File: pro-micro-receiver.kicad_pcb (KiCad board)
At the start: 4 copper layers, 40 parts, among them J1 USB_A_PLUG, J2 Conn_01x04, SW1 SW_Push, U1 TLV740P, U2 ATmega32U4-M, U3 YJ-14015, Y1 16MHz

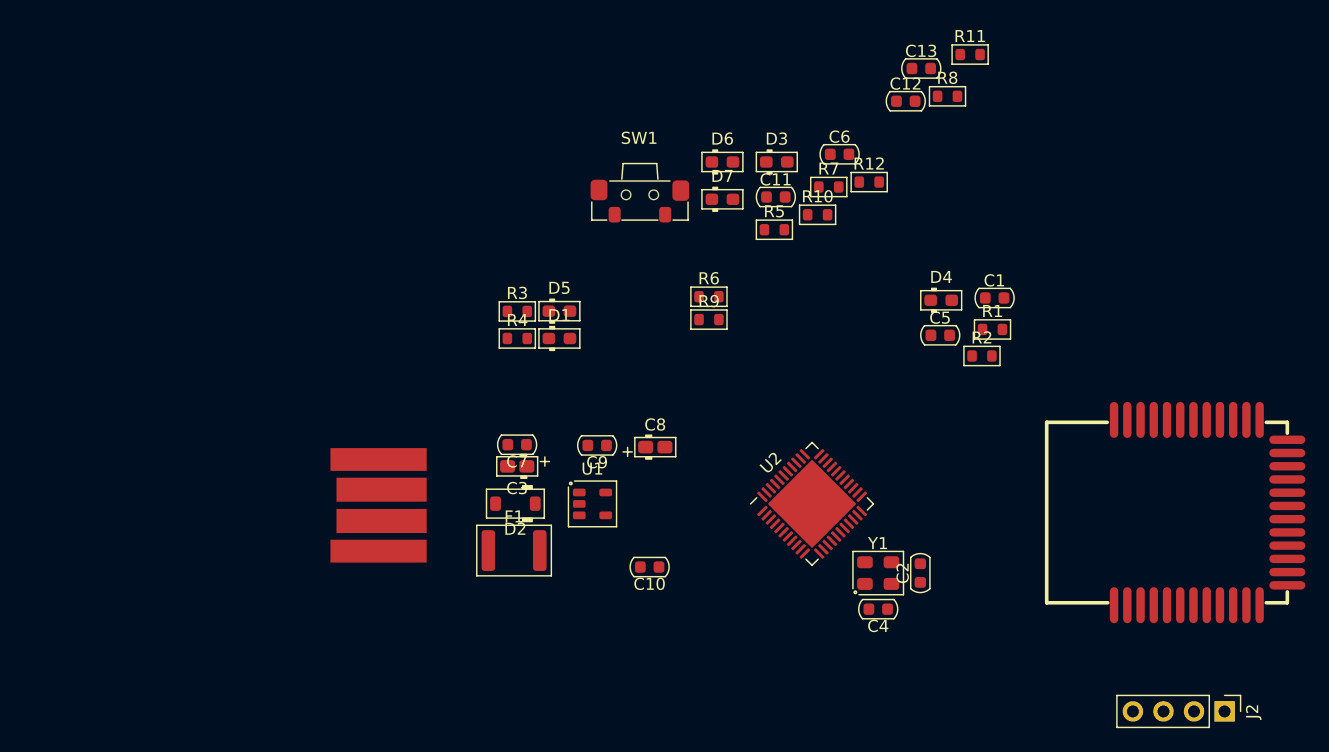
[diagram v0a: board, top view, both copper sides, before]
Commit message: Fixing the stackup Adding initial board outline Moving all elements onto the board
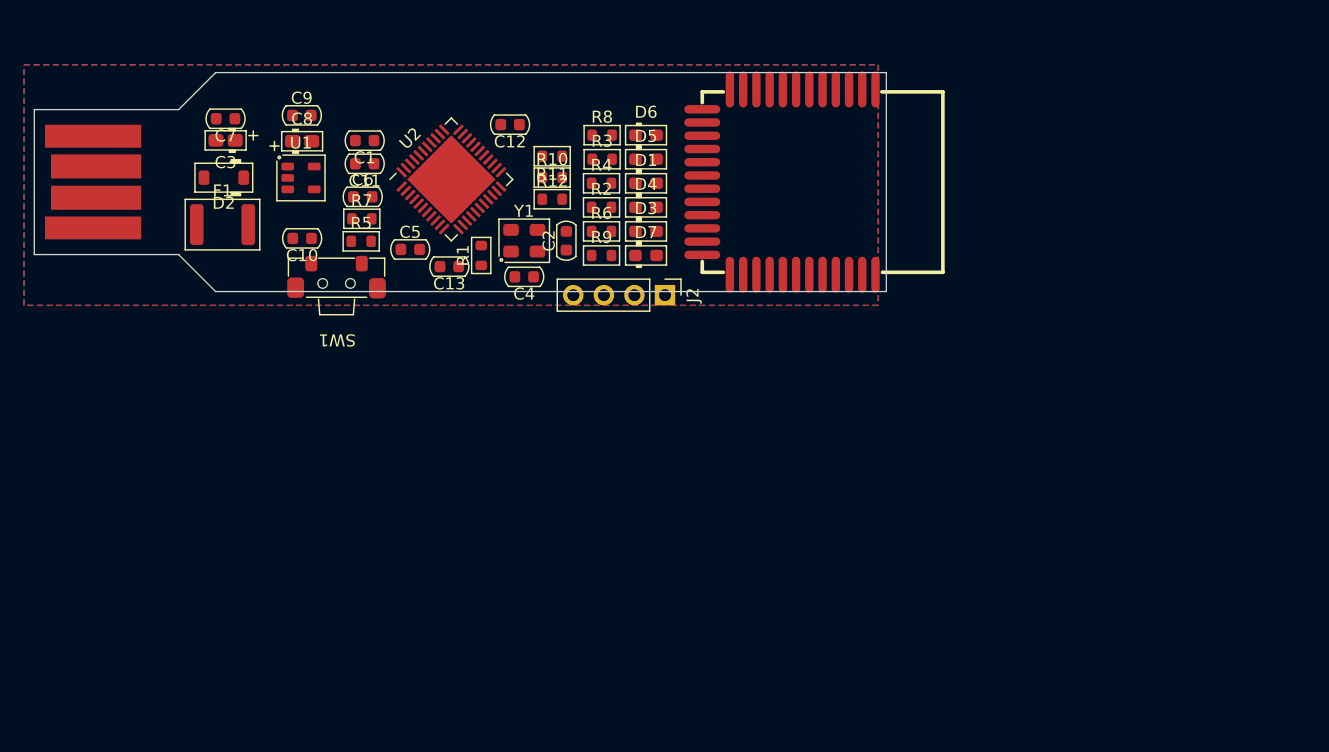
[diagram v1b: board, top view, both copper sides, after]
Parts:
- moved J2 58.0 mm to (113.3, 83.2)
- moved C1 54.0 mm to (88.3, 70.3), turned to 180 degrees
- moved C5 44.6 mm to (92.1, 79.3)
- moved R1 42.9 mm to (98.0, 79.8), turned to 90 degrees
- moved C13 42.5 mm to (95.3, 80.8), turned to 180 degrees
- moved C2 40.4 mm to (105.1, 78.6)
- moved C4 40.4 mm to (101.6, 81.6)
- moved Y1 40.4 mm to (101.6, 78.6)
- moved U2 40.3 mm to (95.5, 73.5)
- moved C6 39.8 mm to (88.2, 75.0)
- moved C10 39.8 mm to (83.1, 78.4)
- moved R7 38.9 mm to (88.1, 76.8)
- moved C8 38.8 mm to (83.1, 70.4)
- moved C9 36.8 mm to (83.1, 68.2), turned to 0 degrees
- moved C3 36.4 mm to (76.8, 70.3)
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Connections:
- net Net-(R5-Pad1) renamed /D+OUT
- net Net-(R7-Pad1) renamed /D-OUT
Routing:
- added copper zone on B.Cu, net GND
- added copper zone on F.Cu, net GND
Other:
- board outline added: 70.8 x 18.2 mm

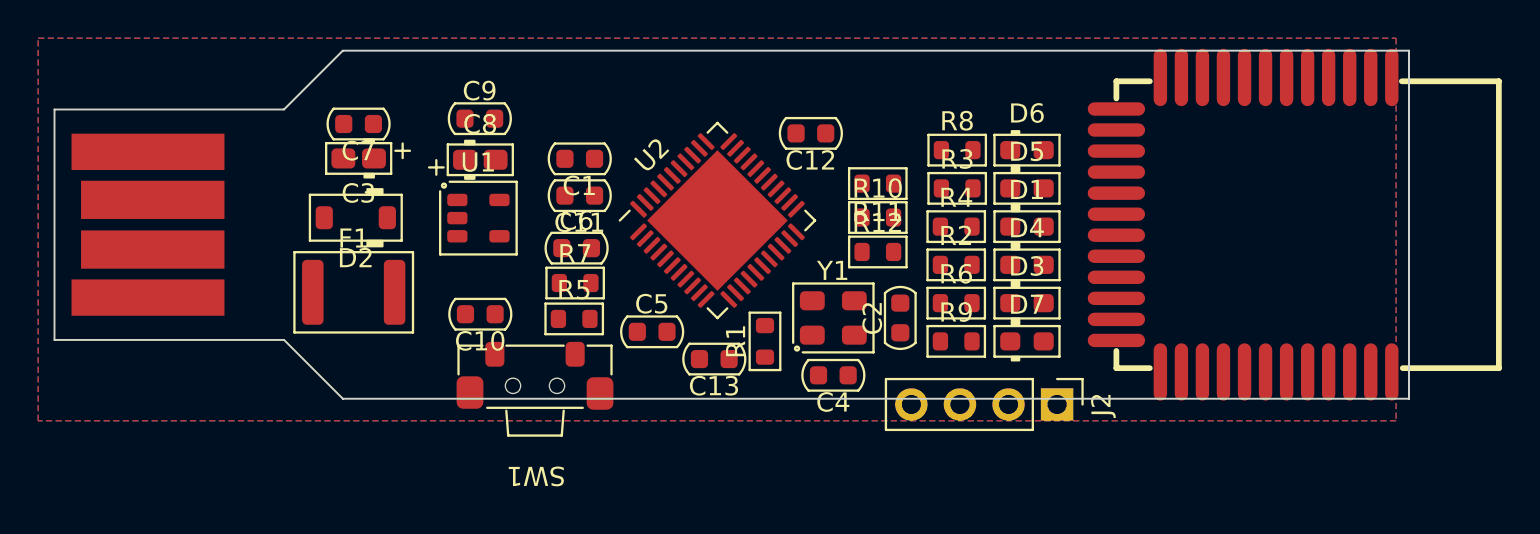
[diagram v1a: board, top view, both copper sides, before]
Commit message: Shortening the board and better placement of components
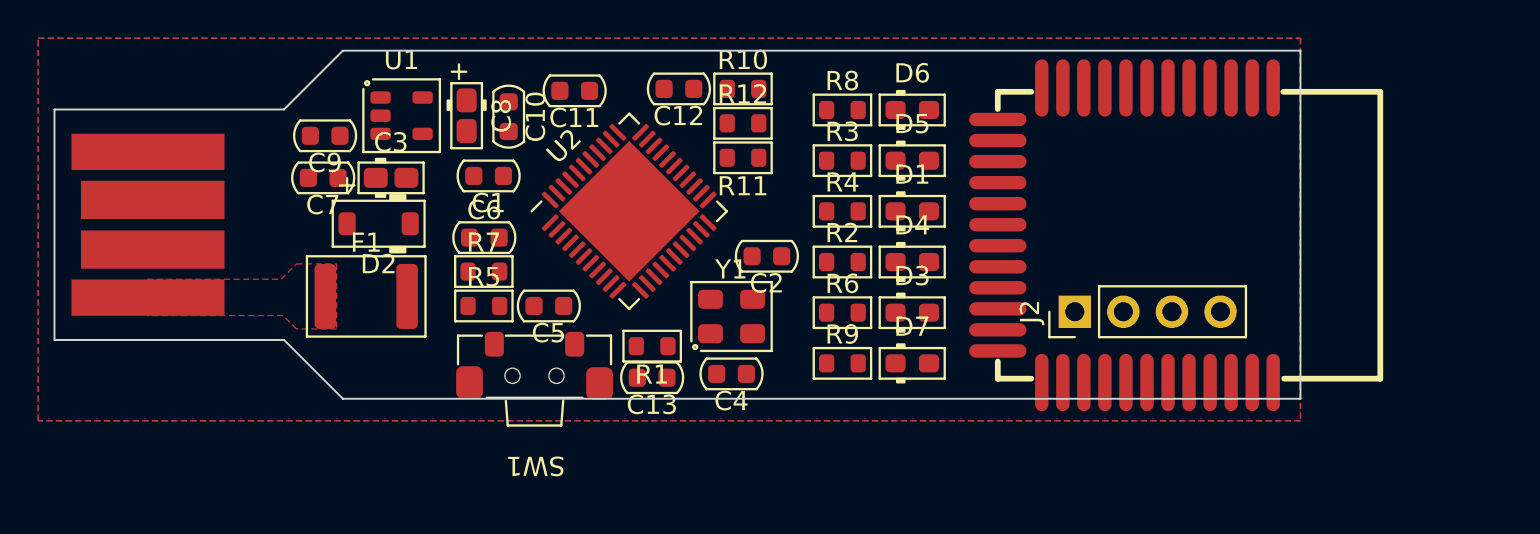
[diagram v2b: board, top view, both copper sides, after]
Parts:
- moved C10 10.4 mm to (84.6, 68.1), turned to -90 degrees
- moved R10 9.74 mm to (96.8, 66.7)
- moved R12 9.74 mm to (96.8, 68.5)
- moved C9 8.14 mm to (75.0, 69.1), turned to 180 degrees
- moved C2 7.68 mm to (98.1, 75.4), turned to 180 degrees
- moved C12 7.28 mm to (93.5, 66.7)
- moved R11 7.18 mm to (96.8, 70.2)
- moved U1 6.69 mm to (79.0, 68.0)
- moved D6 6.36 mm to (105.7, 67.8)
- moved R8 6.36 mm to (102.0, 67.8)
- moved U3 6.22 mm to (130.2, 74.3)
- moved D5 6.17 mm to (105.7, 70.4)
- moved R3 6.17 mm to (102.0, 70.4)
- moved D7 6.11 mm to (105.7, 81.0)
- moved R9 6.06 mm to (102.0, 81.0)
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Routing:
- added copper zone on F.Cu, net UVCC
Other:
- board size 70.8 x 18.2 mm -> 65.2 x 18.2 mm

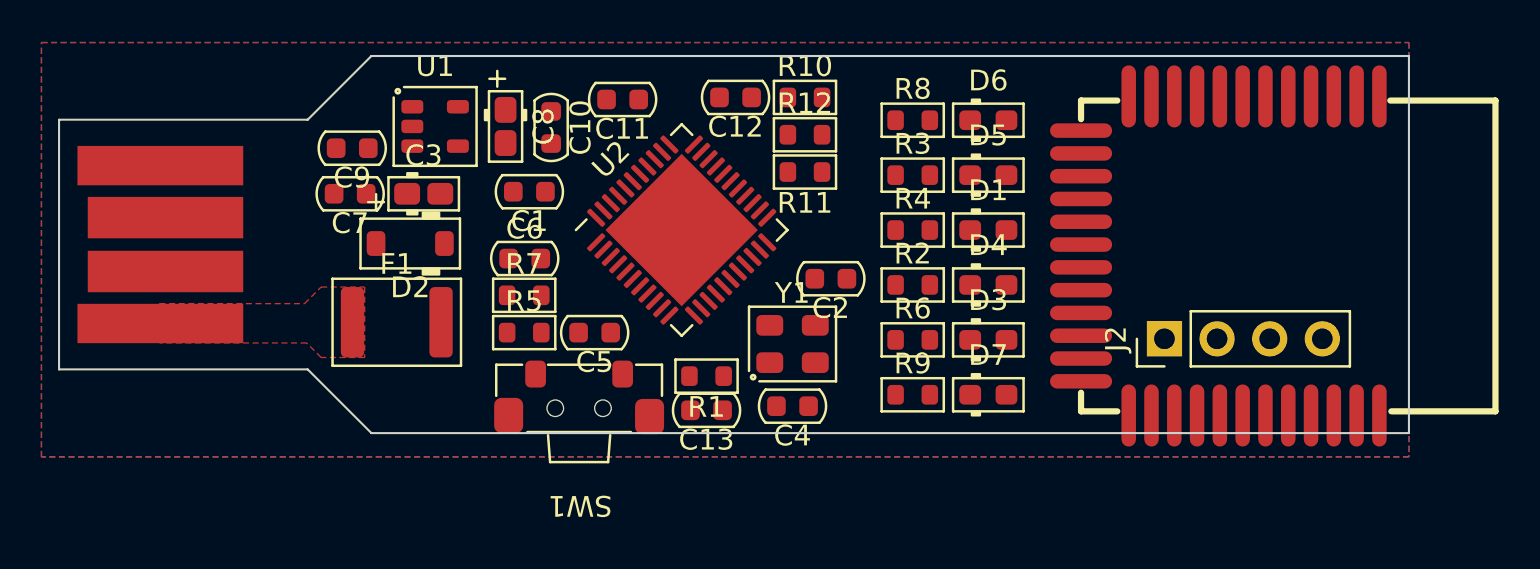
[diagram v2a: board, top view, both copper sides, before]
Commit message: Compacting the board
Shifting the crystal and the components to shorten the board
Distancing the elements from the edge
Rounding the corners
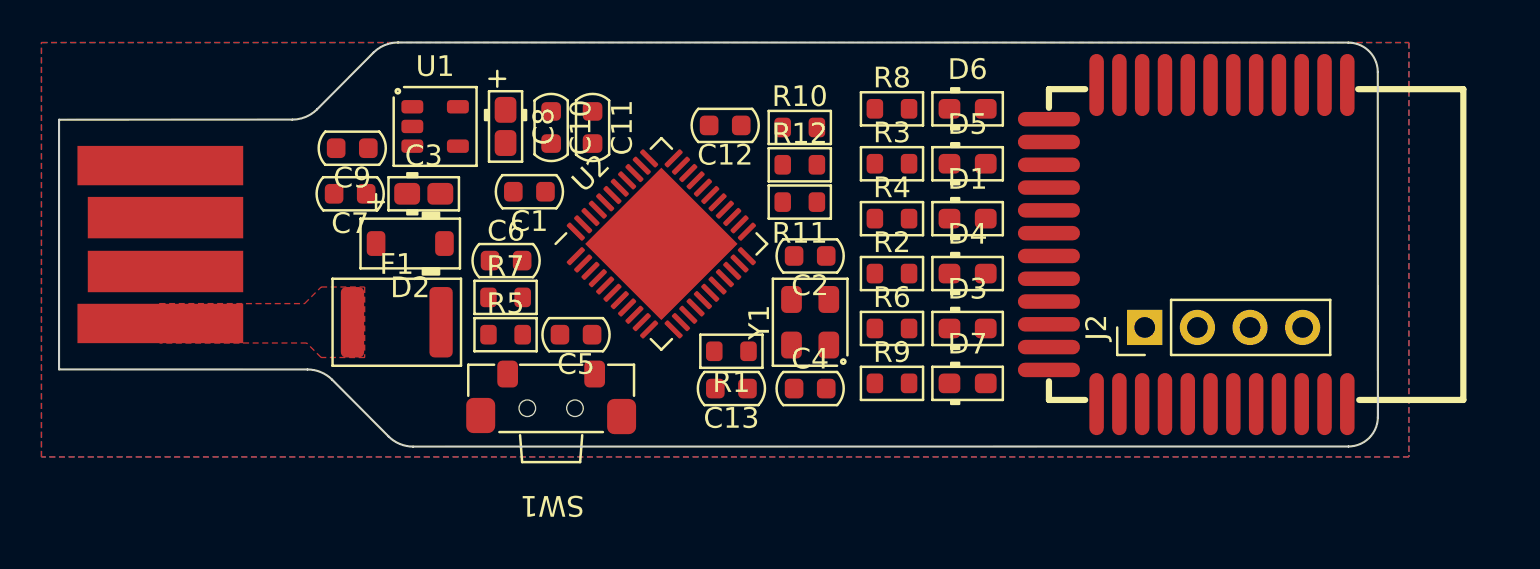
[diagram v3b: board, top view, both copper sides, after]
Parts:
- moved C11 1.98 mm to (86.6, 68.1), turned to -90 degrees
- moved R1 1.70 mm to (93.3, 78.9)
- moved U3 1.64 mm to (128.6, 73.8)
- moved C13 1.59 mm to (93.3, 80.7)
- moved C2 1.49 mm to (97.1, 74.3)
- moved R11 1.47 mm to (96.6, 71.7)
- moved R12 1.47 mm to (96.6, 69.9)
- moved R10 1.47 mm to (96.6, 68.1)
- moved C12 1.44 mm to (93.0, 68.0)
- moved Y1 1.35 mm to (97.1, 77.5), turned to 90 degrees
- moved SW1 1.35 mm to (84.6, 81.0)
- moved C4 1.20 mm to (97.1, 80.7), turned to 0 degrees
- moved U2 1.19 mm to (89.9, 73.7)
- moved D5 1.14 mm to (104.7, 69.8)
- moved R3 1.14 mm to (101.0, 69.8)
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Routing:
- added copper zone on In1.Cu, net GND
- added copper zone on In2.Cu, net VCC
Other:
- board size 65.2 x 18.2 mm -> 63.6 x 19.5 mm

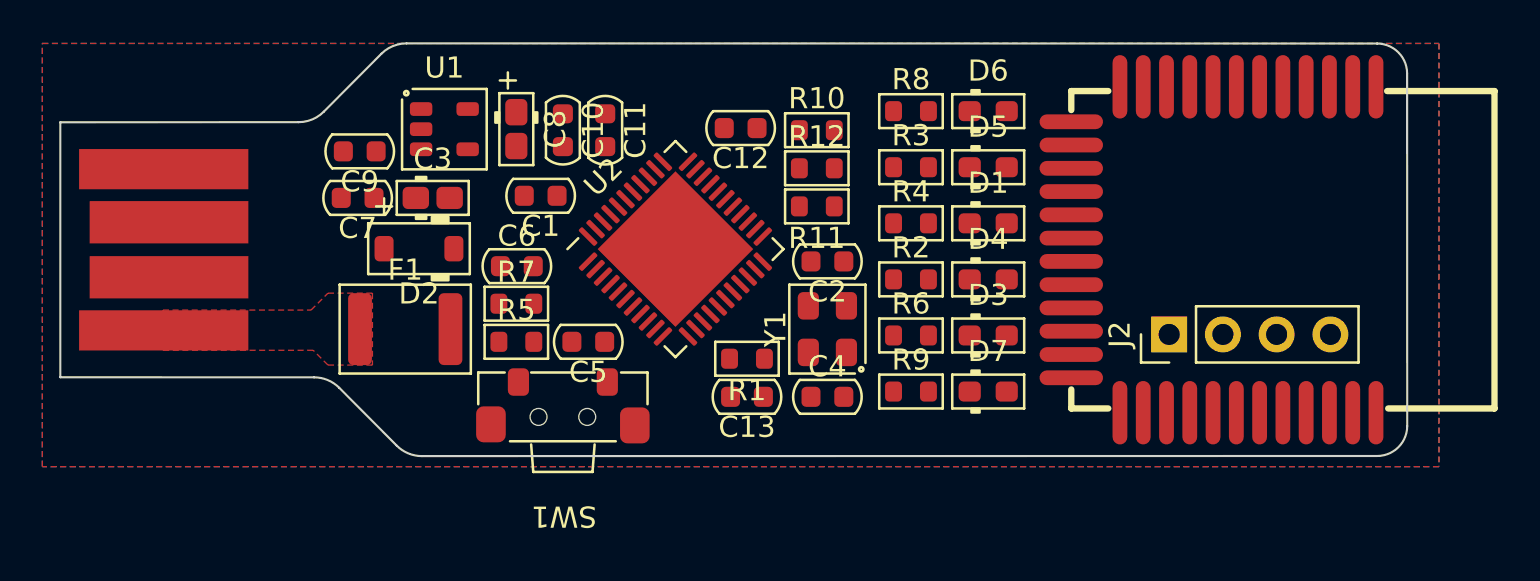
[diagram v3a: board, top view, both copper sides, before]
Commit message: Completed routing board
Removed all designators from silkscreen
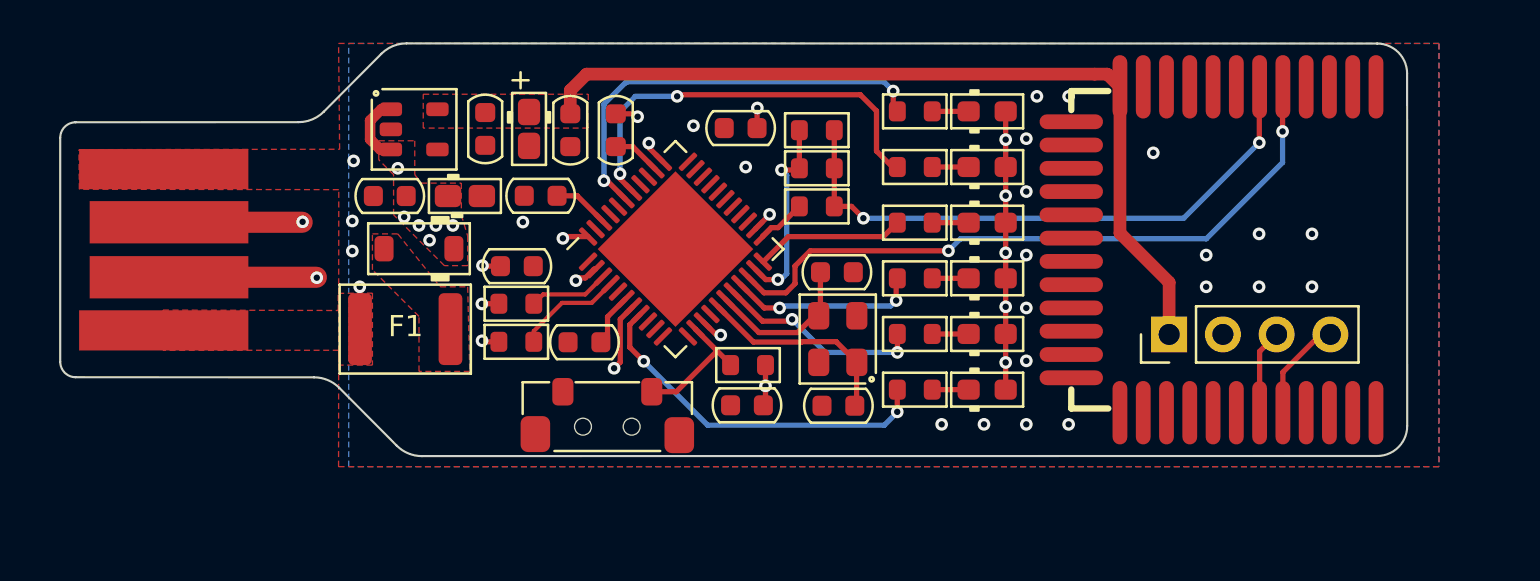
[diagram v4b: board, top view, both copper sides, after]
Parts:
- moved R9 10.6 mm to (101.2, 69.8)
- moved D7 10.6 mm to (104.7, 69.8)
- moved R4 7.86 mm to (101.2, 80.4)
- moved D1 7.86 mm to (104.7, 80.4)
- moved C9 6.02 mm to (80.9, 68.0), turned to -90 degrees
- moved R6 5.33 mm to (101.2, 72.5)
- moved D3 5.33 mm to (104.7, 72.5)
- moved R3 5.25 mm to (101.2, 75.1)
- moved D5 5.25 mm to (104.7, 75.1)
- moved R2 2.59 mm to (101.2, 77.7)
- moved D4 2.58 mm to (104.7, 77.7)
- moved SW1 2.15 mm to (86.7, 81.5)
- moved C3 1.52 mm to (80.0, 71.2)
- moved C7 1.52 mm to (76.4, 71.2)
- moved U1 1.43 mm to (77.6, 68.1)
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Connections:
- net Net-(D2-Pad2) renamed /FUSED
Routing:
- net +3V3: track 0.00 -> 40.3 mm
- net RXI: track 0.00 -> 32.2 mm, vias 0 -> 2
- net TXODIV: track 0.00 -> 28.0 mm, vias 0 -> 2
- net UVCC: track 0.00 -> 26.6 mm, vias 0 -> 4
- net VCC: track 0.00 -> 24.9 mm, vias 0 -> 18
- net /C_A3: track 0.00 -> 20.3 mm, vias 0 -> 2
- net /D+OUT: track 0.00 -> 20.0 mm, vias 0 -> 2
- net /C_A2: track 0.00 -> 19.8 mm, vias 0 -> 2
- net /TX_LED: track 0.00 -> 17.3 mm, vias 0 -> 2
- net /D-OUT: track 0.00 -> 16.1 mm, vias 0 -> 2
- net /C_D3: track 0.00 -> 9.90 mm, vias 0 -> 2
- net Net-(C4-Pad2): track 0.00 -> 9.76 mm
- net TXO: track 0.00 -> 9.49 mm, vias 0 -> 2
- net /C_D2: track 0.00 -> 8.97 mm, vias 0 -> 2
- net Net-(C2-Pad2): track 0.00 -> 7.49 mm
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- added copper zone on F.Cu, net +3V3
- added copper zone on F.Cu, net /FUSED
- added copper zone on F.Cu, net VCC
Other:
- board size 63.6 x 19.5 mm -> 63.7 x 19.5 mm
